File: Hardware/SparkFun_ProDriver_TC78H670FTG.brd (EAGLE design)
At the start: 50.8 x 57.1 mm, 87 parts, among them J2 LATCH, J3 PTH, J4 LATCH, J5 LATCH, J6 PTH, J7 LATCH, J8 PTH, U1 TC78H670FTG

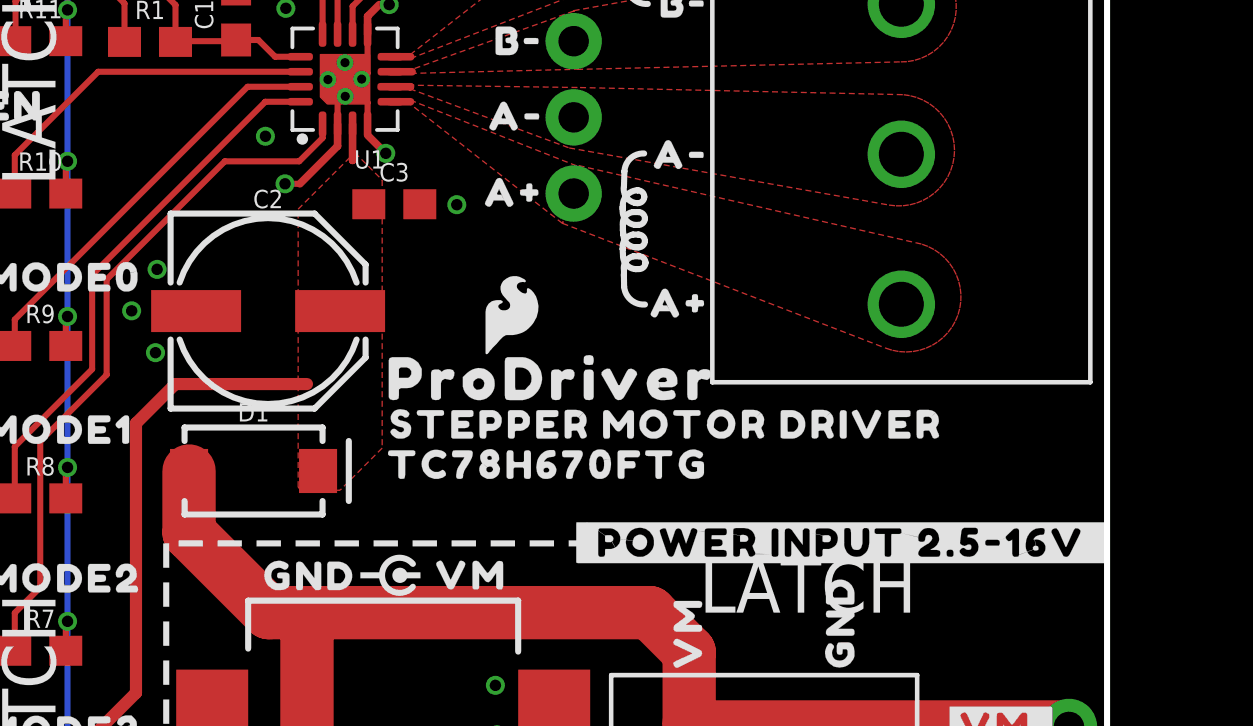
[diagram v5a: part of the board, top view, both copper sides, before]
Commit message: Added PTC and 0Ohm res to power input
plus bypass jumpers down below
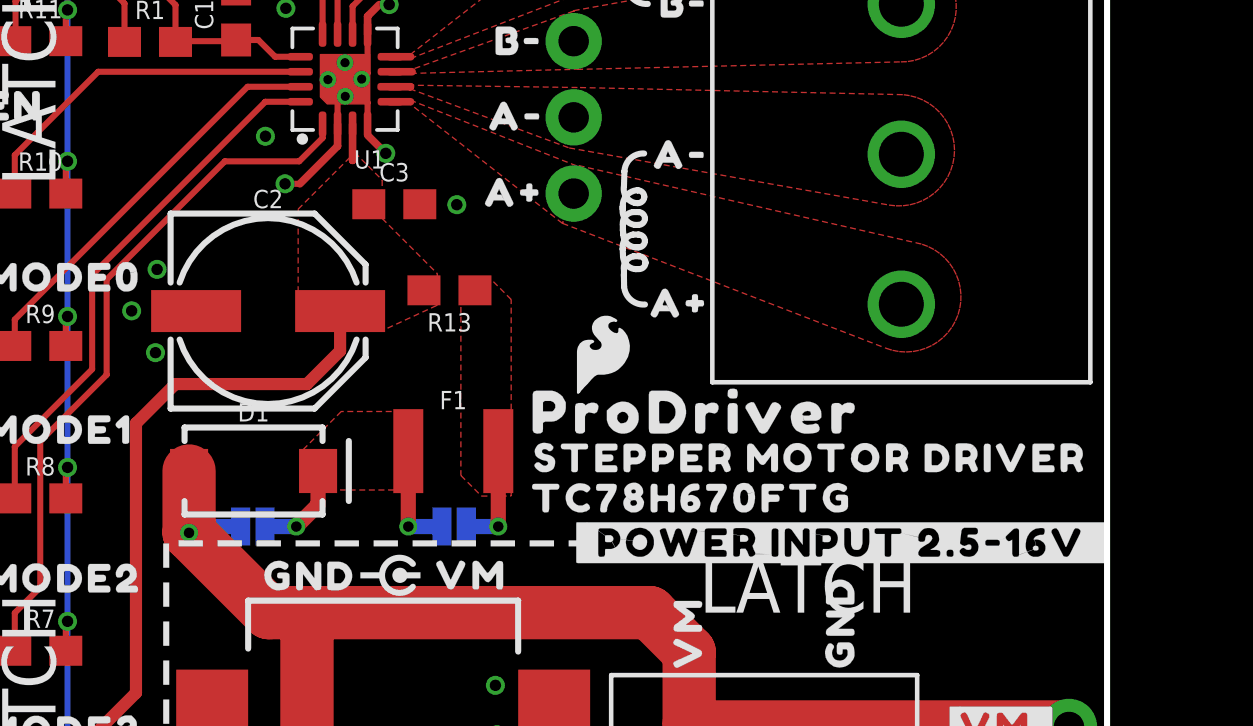
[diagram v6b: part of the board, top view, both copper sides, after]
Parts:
- added F1: 16V/1.1A(2.2A TRIP), TC78H670FTG:1210
- added JP2, JP3: (no value), SparkFun-Jumpers:SMT-JUMPER_2_NO_SILK
- added R13: 0, SparkFun-Resistors:0603
- added U$38: (no value), output:#D1_BP#0
- added U$39: (no value), output:#PTC_BP#0
- moved U$40 4.93 mm to (30.6, 21.9)
- moved U$6 4.93 mm to (30.9, 19.1)
- moved U$9 4.93 mm to (31.0, 20.4)
- moved LOGO4 3.32 mm to (34.0, 23.9)
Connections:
- new net N$1: D1.C, F1.1, JP2.1, JP3.2
- new net N$3: F1.2, JP2.2, R13.1
- net RAW: now also JP3.1
- net VM: now also R13.2; no longer D1.C
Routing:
- net N$1: track 0.00 -> 6.83 mm, vias 0 -> 2
- net N$3: track 0.00 -> 3.58 mm, vias 0 -> 1
- net VM: track 29.4 -> 32.3 mm
- net RAW: track 52.1 -> 53.9 mm, vias 0 -> 1
- added copper zone on layer 1, net N$1
- added copper zone on layer 1, net N$3
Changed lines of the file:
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@@
 <layer number="39" name="tKeepout" color="4" fill="11" visible="no" active="yes"/>
 <layer number="40" name="bKeepout" color="1" fill="11" visible="no" active="yes"/>
-<layer number="41" name="tRestrict" color="4" fill="10" visible="yes" active="yes"/>
+<layer number="41" name="tRestrict" color="4" fill="10" visible="no" active="yes"/>
 <layer number="42" name="bRestrict" color="1" fill="10" visible="no" active="yes"/>
 <layer number="43" name="vRestrict" color="2" fill="10" visible="no" active="yes"/>
@@
 <attribute name="REV" value="" x="-2.54" y="-16.51" size="1.778" layer="27" display="off"/>
 </element>
-<element name="LOGO4" library="SparkFun-Aesthetics" package="SFE_LOGO_FLAME_.1" value="SFE_LOGO_FLAME.1_INCH" x="30.94228125" y="25.181553125" smashed="yes"/>
+<element name="LOGO4" library="SparkFun-Aesthetics" package="SFE_LOGO_FLAME_.1" value="SFE_LOGO_FLAME.1_INCH" x="33.99028125" y="23.860753125" smashed="yes"/>
 <element name="FID3" library="SparkFun-Aesthetics" package="FIDUCIAL-1X2" value="FIDUCIAL1X2" x="4.904740625" y="56.243221875" smashed="yes" rot="MR0"/>
 <element name="FID4" library="SparkFun-Aesthetics" package="FIDUCIAL-1X2" value="FIDUCIAL1X2" x="45.907959375" y="0.942340625" smashed="yes" rot="MR0"/>
@@
 <element name="U$29" library="output" package="GND6" value="" x="21.9964" y="16.4592" smashed="yes"/>
 <element name="U$30" library="output" package="VM10" value="" x="27.7368" y="16.4846" smashed="yes"/>
-<element name="U$6" library="output" package="TC78H670FTG0" value="" x="26.134053125" y="20.170134375" smashed="yes"/>
-<element name="U$9" library="output" package="STEPPER_MOTOR_DRIVER0" value="" x="26.200090625" y="21.511253125" smashed="yes"/>
+<element name="U$6" library="output" package="TC78H670FTG0" value="" x="30.934653125" y="19.052534375" smashed="yes"/>
+<element name="U$9" library="output" package="STEPPER_MOTOR_DRIVER0" value="" x="31.000690625" y="20.393653125" smashed="yes"/>
 <element name="U$31" library="output" package="#GND#0" value="" x="13.9954" y="55.5498" smashed="yes" rot="R270"/>
-<element name="U$40" library="output" package="PRODRIVER0" value="" x="25.75559375" y="23.03525625" smashed="yes"/>
+<element name="U$40" library="output" package="PRODRIVER0" value="" x="30.55619375" y="21.91765625" smashed="yes"/>
 <element name="U$41" library="output" package="#_POWER_INPUT_2#5#16V_#0" value="" x="32.766" y="17.571721875" smashed="yes"/>
 <element name="U$14" library="output" package="#MTR#0" value="" x="37.79011875" y="48.907696875" smashed="yes"/>
@@
 <element name="U$7" library="output" package="#ERR#7" value="" x="19.1262" y="55.5498" smashed="yes" rot="R270"/>
 <element name="U$32" library="output" package="#VREF#0" value="" x="36.83" y="55.4736" smashed="yes" rot="R270"/>
+<element name="F1" library="TC78H670FTG" package="1210" value="16V/1.1A(2.2A TRIP)" x="29.0068" y="20.6248" smashed="yes">
+<attribute name="NAME" x="29.0068" y="22.0218" size="0.6096" layer="25" font="vector" ratio="20" align="bottom-center"/>
+<attribute name="PROD_ID" value="RES-15179" x="29.0068" y="20.6248" size="1.778" layer="27" display="off"/>
+<attribute name="VALUE" x="29.0068" y="19.2278" size="0.6096" layer="27" font="vector" ratio="20" align="top-center"/>
+</element>
+<element name="R13" library="SparkFun-Resistors" library_urn="urn:adsk.eagle:library:532" package="0603" package3d_urn="urn:adsk.eagle:package:39650/1" value="0" x="28.8798" y="25.9842" smashed="yes" rot="R180">
+<attribute name="NAME" x="28.8798" y="25.2222" size="0.6096" layer="25" font="vector" ratio="20" rot="R180" align="bottom-center"/>
+<attribute name="PROD_ID" value="RES-08609" x="28.8798" y="25.9842" size="1.778" layer="27" rot="R180" display="off"/>
+<attribute name="VALUE" x="28.8798" y="26.7462" size="0.6096" layer="27" font="vector" ratio="20" rot="R180" align="top-center"/>
+</element>
+<element name="JP2" library="SparkFun-Jumpers" library_urn="urn:adsk.eagle:library:528" package="SMT-JUMPER_2_NO_SILK" package3d_urn="urn:adsk.eagle:package:39279/1" value="" x="29.0322" y="18.1102" smashed="yes" rot="MR180">
+<attribute name="NAME" x="29.0322" y="16.9672" size="0.6096" layer="26" font="vector" ratio="20" rot="MR180" align="bottom-center"/>
+<attribute name="VALUE" x="29.0322" y="19.2532" size="0.6096" layer="28" font="vector" ratio="20" rot="MR180" align="top-center"/>
+</element>
+<element name="JP3" library="SparkFun-Jumpers" library_urn="urn:adsk.eagle:library:528" package="SMT-JUMPER_2_NO_SILK" package3d_urn="urn:adsk.eagle:package:39279/1" value="" x="22.3266" y="18.1102" smashed="yes" rot="MR180">
+<attribute name="NAME" x="22.3266" y="16.9672" size="0.6096" layer="26" font="vector" ratio="20" rot="MR180" align="bottom-center"/>
+<attribute name="VALUE" x="22.3266" y="19.2532" size="0.6096" layer="28" font="vector" ratio="20" rot="MR180" align="top-center"/>
+</element>
+<element name="U$38" library="output" package="#D1_BP#0" value="" x="21.5138" y="18.0594" smashed="yes" rot="MR0"/>
+<element name="U$39" library="output" package="#PTC_BP#0" value="" x="36.5252" y="18.1102" smashed="yes" rot="MR0"/>
 </elements>
 <signals>
@@
 <contactref element="C2" pad="+"/>
 <contactref element="C3" pad="1"/>
-<contactref element="D1" pad="C"/>
 <contactref element="U2" pad="3"/>
 <polygon width="0.2032" layer="1" thermals="no">
-<vertex x="23.835359375" y="19.42338125"/>
+<vertex x="23.835359375" y="24.64054375"/>
 <vertex x="23.835359375" y="28.689309375"/>
 <vertex x="25.722571875" y="30.576521875"/>
 <vertex x="26.63698125" y="29.6621125"/>
-<vertex x="26.63698125" y="20.726403125"/>
-<vertex x="25.22981875" y="19.319240625"/>
-<vertex x="23.9395" y="19.319240625"/>
+<vertex x="26.63698125" y="28.37941875"/>
+<vertex x="28.4734" y="26.543"/>
+<vertex x="28.4734" y="25.5016"/>
+<vertex x="28.448" y="25.4762"/>
+<vertex x="26.63698125" y="24.64054375"/>
 </polygon>
 <wire x1="25.65" y1="31.522" x2="25.65" y2="30.316359375" width="0.254" layer="1"/>
@@
 <wire x1="16.9900625" y1="11.1252" x2="12.6492" y2="11.1252" width="0.4064" layer="1"/>
 <wire x1="11.176" y1="7.366" x2="11.5316" y2="7.0104" width="0.4064" layer="1"/>
+<contactref element="R13" pad="2"/>
+<wire x1="24.13" y1="22.86" x2="25.2346" y2="23.9646" width="0.4064" layer="1"/>
+<wire x1="25.2346" y1="23.9646" x2="25.2346" y2="25.29331875" width="0.4064" layer="1"/>
 </signal>
 <signal name="OUT_A+">
@@
 <wire x1="24.13" y1="15.24" x2="24.13" y2="6.858" width="1.778" layer="1"/>
 <wire x1="24.13" y1="6.858" x2="23.114" y2="5.842" width="1.778" layer="1"/>
+<contactref element="JP3" pad="1"/>
+<wire x1="21.9202" y1="18.1102" x2="20.40911875" y2="18.1102" width="0.508" layer="16"/>
+<wire x1="20.40911875" y1="18.1102" x2="20.199459375" y2="17.900540625" width="0.508" layer="16"/>
+<via x="20.199459375" y="17.900540625" extent="1-16" drill="0.35"/>
 </signal>
 <signal name="N$4">
@@
 <wire x1="30.06" y1="45.3136" x2="30.0346" y2="45.339" width="0.2032" layer="1"/>
 </signal>
+<signal name="N$1">
+<contactref element="D1" pad="C"/>
+<contactref element="F1" pad="1"/>
+<contactref element="JP3" pad="2"/>
+<contactref element="JP2" pad="1"/>
+<wire x1="27.5068" y1="20.6248" x2="27.5068" y2="18.1116" width="0.508" layer="1"/>
+<wire x1="27.5068" y1="18.1116" x2="27.5082" y2="18.1102" width="0.508" layer="1"/>
+<via x="27.5082" y="18.1102" extent="1-16" drill="0.35"/>
+<wire x1="27.5082" y1="18.1102" x2="28.6258" y2="18.1102" width="0.508" layer="16"/>
+<polygon width="0.2032" layer="1" thermals="no">
+<vertex x="27.9146" y="21.9456"/>
+<vertex x="25.273" y="21.9456"/>
+<vertex x="23.9522" y="20.6248"/>
+<vertex x="23.9522" y="19.3294"/>
+<vertex x="27.9146" y="19.3294"/>
+</polygon>
+<wire x1="24.499459375" y1="19.961859375" x2="24.499459375" y2="18.835259375" width="0.508" layer="1"/>
+<wire x1="24.499459375" y1="18.835259375" x2="23.7744" y2="18.1102" width="0.508" layer="1"/>
+<via x="23.7744" y="18.1102" extent="1-16" drill="0.35"/>
+<wire x1="23.7744" y1="18.1102" x2="22.733" y2="18.1102" width="0.508" layer="16"/>
+</signal>
+<signal name="N$3">
+<contactref element="F1" pad="2"/>
+<contactref element="JP2" pad="2"/>
+<contactref element="R13" pad="1"/>
+<polygon width="0.2032" layer="1" thermals="no">
+<vertex x="29.2608" y="26.3906"/>
+<vertex x="29.2608" y="19.812"/>
+<vertex x="29.9466" y="19.1262"/>
+<vertex x="30.9372" y="19.1262"/>
+<vertex x="30.9372" y="25.6794"/>
+<vertex x="30.226" y="26.3906"/>
+</polygon>
+<wire x1="30.5068" y1="20.6248" x2="30.5068" y2="18.1116" width="0.508" layer="1"/>
+<wire x1="30.5068" y1="18.1116" x2="30.5054" y2="18.1102" width="0.508" layer="1"/>
+<via x="30.5054" y="18.1102" extent="1-16" drill="0.35"/>
+<wire x1="30.5054" y1="18.1102" x2="29.4386" y2="18.1102" width="0.508" layer="16"/>
+</signal>
 </signals>
 <mfgpreviewcolors>
@@
 </drawing>
 <compatibility>
+<note version="8.2" severity="warning">
+Since Version 8.2, EAGLE supports online libraries. The ids
+of those online libraries will not be understood (or retained)
+with this version.
+</note>
 <note version="8.3" severity="warning">
 Since Version 8.3, EAGLE supports URNs for individual library

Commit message: added value to lm1117 so it's visible in sch
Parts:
- U2: value (none) -> LM1117
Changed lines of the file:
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@@
 <attribute name="VALUE" x="22.349459375" y="18.310859375" size="0.6096" layer="27" font="vector" ratio="20" align="top-center"/>
 </element>
-<element name="U2" library="SparkFun-IC-Power" package="SOT223" value="" x="10.1346" y="4.699" smashed="yes" rot="R90">
+<element name="U2" library="SparkFun-IC-Power" package="SOT223" value="LM1117" x="10.1346" y="4.699" smashed="yes" rot="R90">
 <attribute name="NAME" x="5.6261" y="3.8735" size="0.4064" layer="25" rot="R90"/>
 <attribute name="PROD_ID" value="VREG-08170" x="10.1346" y="4.699" size="1.778" layer="27" font="vector" ratio="15" rot="R90" display="off"/>
